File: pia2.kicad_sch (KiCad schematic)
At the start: 40 parts, among them IC25 LM393P, IC31 74LS02N, IC34 MC14050BCP, IC35 MC6821

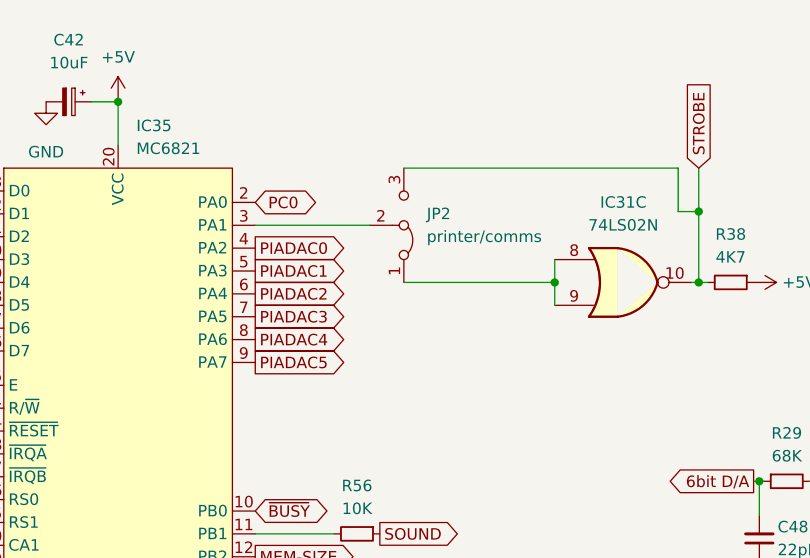
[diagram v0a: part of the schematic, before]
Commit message: rework keyboard type selection
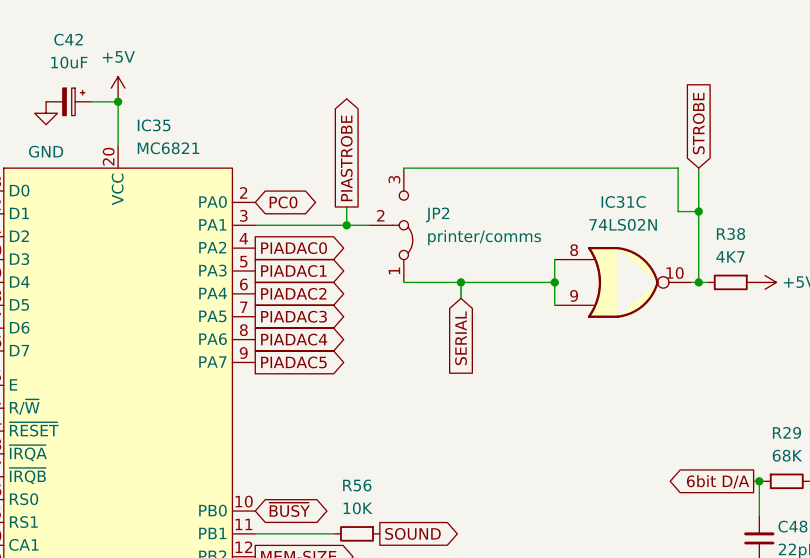
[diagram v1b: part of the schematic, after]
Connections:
- net SERIAL: now reaches IC31.8, IC31.9, JP2.1 (A)
- net PIASTROBE: now reaches IC35.3 (PA1), JP2.2 (C)
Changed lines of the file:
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@@
+	)
+	(junction
+		(at 85.09 40.132)
+		(diameter 0)
+		(color 0 0 0 0)
 	)
 	(junction
@@
 	(junction
 		(at 342.646 46.99)
+		(diameter 0)
+		(color 0 0 0 0)
+	)
+	(junction
+		(at 97.79 46.482)
 		(diameter 0)
 		(color 0 0 0 0)
@@
 	(wire
 		(pts
-			(xy 87.63 40.132) (xy 74.93 40.132)
+			(xy 87.63 40.132) (xy 85.09 40.132)
 		)
 		(stroke
@@
 	(wire
 		(pts
+			(xy 97.79 48.26) (xy 97.79 46.482)
+		)
+		(stroke
+			(width 0)
+			(type default)
+		)
+	)
+	(wire
+		(pts
 			(xy 166.243 32.131) (xy 166.243 44.45)
 		)
@@
 	(wire
 		(pts
+			(xy 85.09 40.132) (xy 74.93 40.132)
+		)
+		(stroke
+			(width 0)
+			(type default)
+		)
+	)
+	(wire
+		(pts
 			(xy 288.163 44.45) (xy 283.21 44.45)
 		)
@@
 	(wire
 		(pts
+			(xy 97.79 46.482) (xy 108.204 46.482)
+		)
+		(stroke
+			(width 0)
+			(type default)
+		)
+	)
+	(wire
+		(pts
 			(xy 151.892 68.58) (xy 151.892 72.39)
 		)
@@
 	(wire
 		(pts
+			(xy 85.09 38.1) (xy 85.09 40.132)
+		)
+		(stroke
+			(width 0)
+			(type default)
+		)
+	)
+	(wire
+		(pts
 			(xy 332.486 36.83) (xy 332.486 31.75)
 		)
@@
 	(wire
 		(pts
-			(xy 91.44 46.482) (xy 108.204 46.482)
+			(xy 91.44 46.482) (xy 97.79 46.482)
 		)
 		(stroke
@@
 		)
 	)
+	(global_label "SERIAL"
+		(shape input)
+		(at 97.79 48.26 270)
+		(fields_autoplaced yes)
+		(effects
+			(font
+				(size 1.27 1.27)
+			)
+			(justify right)
+		)
+		(property "Intersheetrefs" "${INTERSHEET_REFS}"
+			(at 97.79 56.941 90)
+			(effects
+				(font
+					(size 1.27 1.27)
+				)
+				(justify right)
+				(hide yes)
+			)
+		)
+	)
 	(global_label "MIC"
 		(shape output)
@@
 			(effects
 				(font
+					(size 1.27 1.27)
+				)
+				(justify left)
+				(hide yes)
+			)
+		)
+	)
+	(global_label "PIASTROBE"
+		(shape output)
+		(at 85.09 38.1 90)
+		(fields_autoplaced yes)
+		(effects
+			(font
+				(size 1.27 1.27)
+			)
+			(justify left)
+		)
+		(property "Intersheetrefs" "${INTERSHEET_REFS}"
+			(at 85.09 25.609 90)
+			(effects
+				(font

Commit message: refresh BOM
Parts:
- IC25: LCSC (none) -> C5209
- IC31: LCSC (none) -> C22374091; SA2120 Sheet 1 (spare) -> (none)
- TR1: LCSC (none) -> C896866
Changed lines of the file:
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@@
 			)
 		)
+		(property "LCSC" "C896866"
+			(at 382.27 53.34 0)
+			(effects
+				(font
+					(size 1.27 1.27)
+				)
+				(hide yes)
+			)
+		)
 		(pin "1"
 		)
@@
 			)
 		)
-		(property "SA2120" "Sheet 1 (spare)"
+		(property "LCSC" "C22374091"
 			(at 115.824 46.482 0)
 			(effects
@@
 			(at 175.006 44.45 0)
 			(effects
+				(font
+					(size 1.27 1.27)
+				)
+				(hide yes)
+			)
+		)
+		(property "LCSC" "C5209"
+			(at 175.006 44.45 0)
+			(effects

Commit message: align versions
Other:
- title: (none) -> Dragon CPU UK Revised
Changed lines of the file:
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@@
 	(paper "A3")
 	(title_block
-		(date "2023-05-25")
-		(rev "3.0")
+		(title "Dragon CPU UK Revised")
+		(date "2025-10-05")
+		(rev "3.3")
+		(comment 1 "Redesign by Julian Brown")
 	)
 	(junction
